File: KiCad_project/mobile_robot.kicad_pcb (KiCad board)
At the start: 2 copper layers, 90 x 62 mm, 136 parts, among them J1 IR, J10 Screw_Terminal_01x02, J11 Barrel_Jack_Switch, J12 Analog sensor, J13 Encoder A, J14 Encoder B, J15 Conn_02x05_Odd_Even, J16 Conn_02x05_Odd_Even, J17 Conn_01x03_Pin, J18 Conn_01x03_Pin, J19 Conn_02x08_Odd_Even, J2 PROGRAMING, J20 i2c, J3 Conn_01x03_Pin, J4 Conn_01x02_Pin, J5 i2c, J6 STLINK, J7 Conn_01x03_Pin, J8 UART (bluetooth), J9 Analog sensor, M1 Motor_DC, M2 Motor_DC, SW1 SW_Reset, SW2 SW_SPDT_321, U1 STM32G431RBTx, U10 TPS54202DDC, U12 TSOP321xx, U2 DRV8870DDA, U4 DRV8870DDA, U7 fuse, U8 TPS5450DDAR, U9 TPS54202DDC, Y1 Crystal_GND24

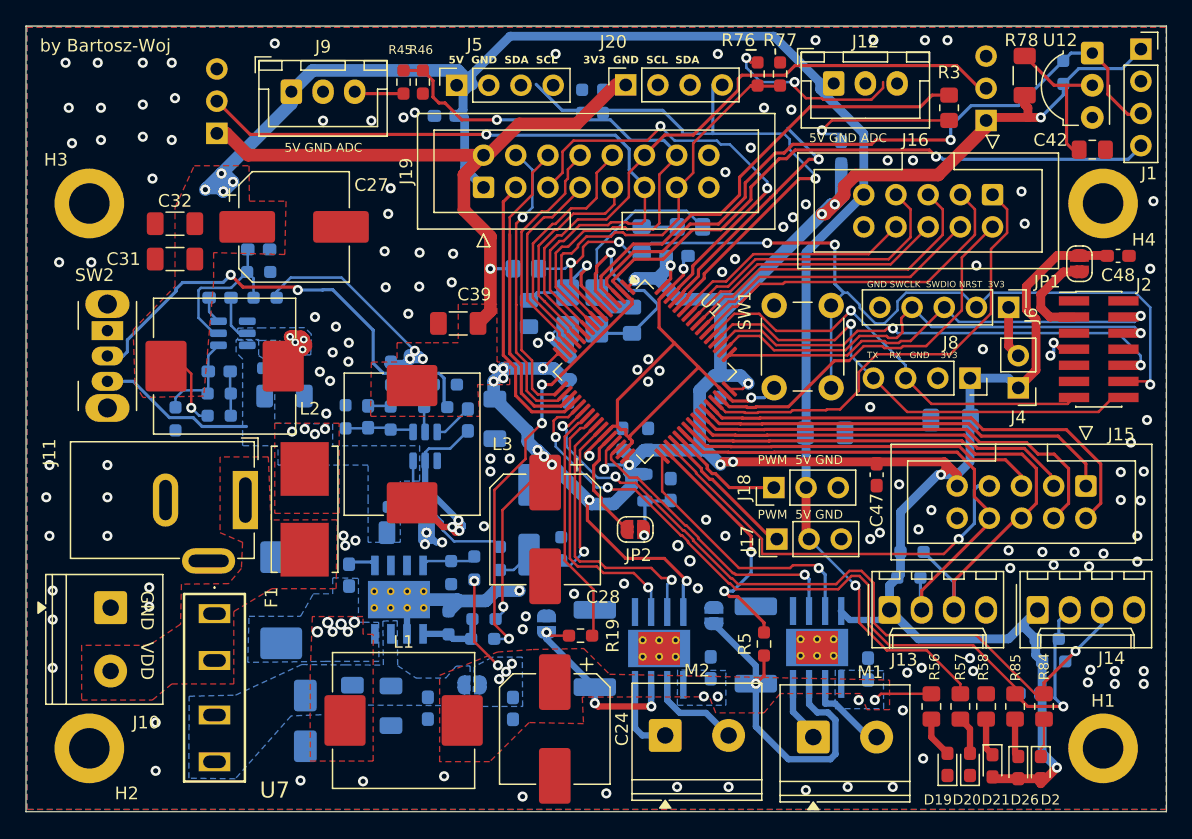
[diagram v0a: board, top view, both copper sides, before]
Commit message: bug solving
- DRC error solving related with I2C pull-up resistors
- updating readme
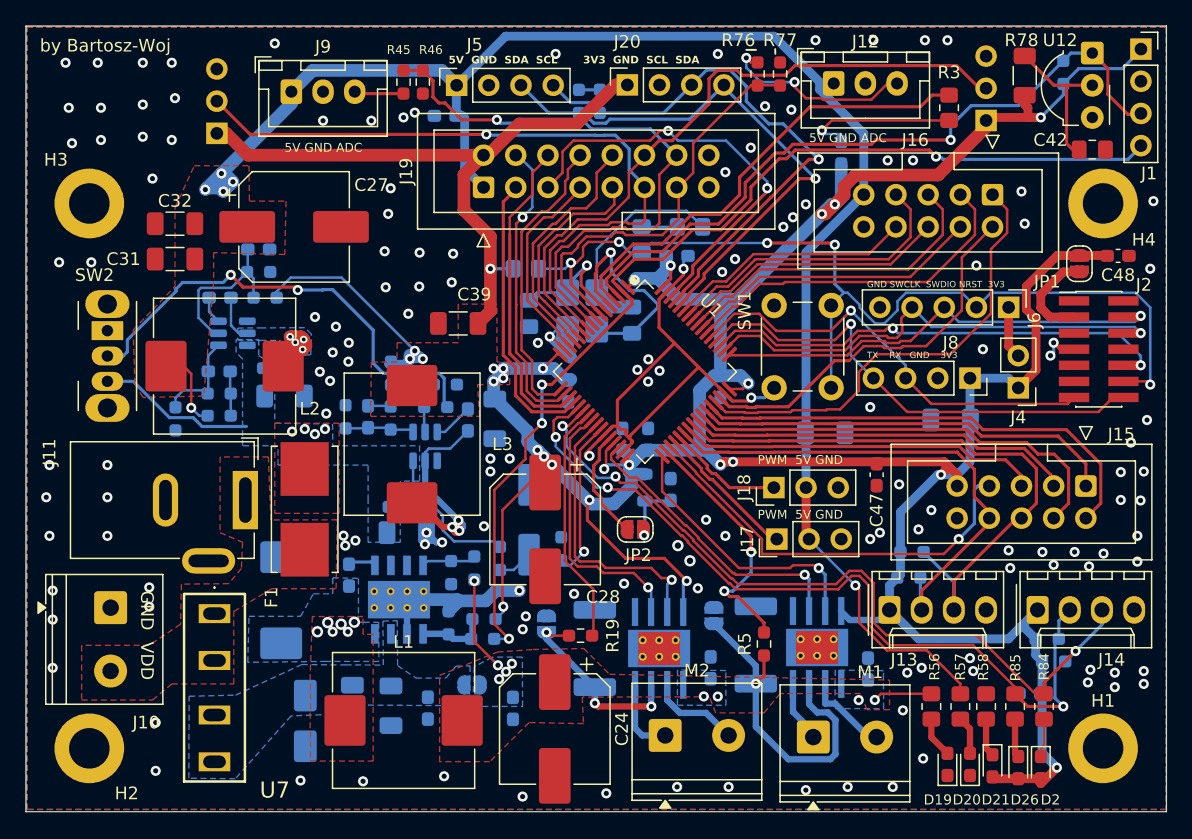
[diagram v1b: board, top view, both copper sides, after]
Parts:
- moved R10 0.25 mm to (145.3, 43.9)
- moved R9 0.25 mm to (143.6, 43.9)
- moved J20 0.13 mm to (147.5, 42.6)
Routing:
- net /i2c_SCL: track 19.8 -> 43.2 mm
- net +3.3V: track 322.2 -> 327.0 mm
- net +5V: track 136.7 -> 135.7 mm
- net /Sensor5: track 51.5 -> 52.4 mm
- net Net-(J12-Pin_3): track 14.2 -> 15.1 mm
- net /i2c_SDA: track 45.0 -> 44.0 mm

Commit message: update routing, changed IR sensor with pinout, rotate right sensor connector (bottom side)
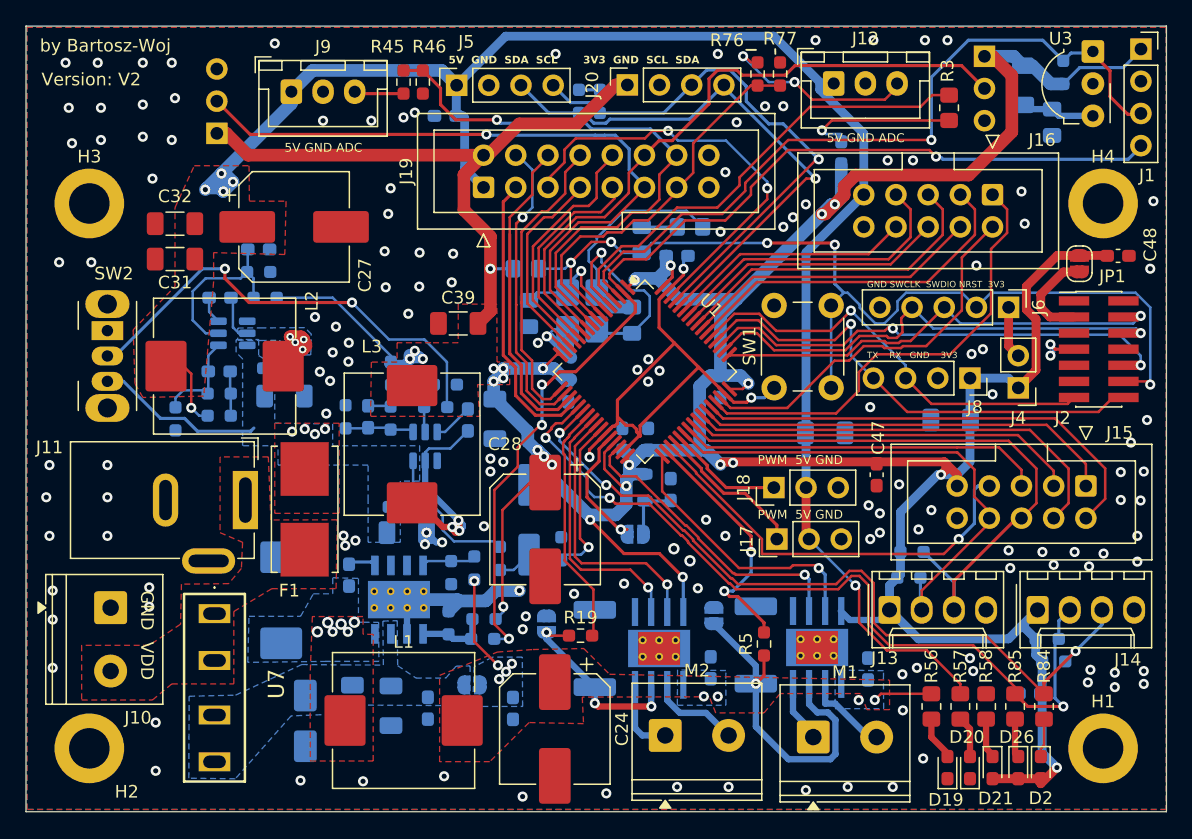
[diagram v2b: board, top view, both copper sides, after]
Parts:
- removed U12: TSOP321xx, footprint_library:Vishay_MOLD-3Pin
- added U3: VS1838B, footprint_library:Vishay_MOLD-3Pin, F.Cu at (184.2, 40.0)
- C1, C3, C4: footprint footprint_library:C_0805_2012Metric_Pad1.18x1.45mm_HandSolder -> Capacitor_SMD:C_0805_2012Metric_Pad1.18x1.45mm_HandSolder
- C11, C2, C22, C23, C25, C26, C30, C33, C34, C35, C37, C40, C44, C46, C47, C48, C9: footprint footprint_library:C_0603_1608Metric_Pad1.08x0.95mm_HandSolder -> Capacitor_SMD:C_0603_1608Metric_Pad1.08x0.95mm_HandSolder
- C20, C21, C29, C31, C32, C36, C38, C39, C41, C45: footprint footprint_library:C_1206_3216Metric_Pad1.33x1.80mm_HandSolder -> Capacitor_SMD:C_1206_3216Metric_Pad1.33x1.80mm_HandSolder
- C24, C27, C28: footprint footprint_library:CP_Elec_8x10.5 -> Capacitor_SMD:CP_Elec_8x10.5
- C42: footprint footprint_library:C_0805_2012Metric_Pad1.18x1.45mm_HandSolder -> Capacitor_SMD:C_0805_2012Metric_Pad1.18x1.45mm_HandSolder; moved to B.Cu
- C43, C5, C6, C7, C8: value C -> 0.1uF; footprint footprint_library:C_0603_1608Metric_Pad1.08x0.95mm_HandSolder -> Capacitor_SMD:C_0603_1608Metric_Pad1.08x0.95mm_HandSolder
- D1, D19, D2, D20, D21, D26: footprint footprint_library:LED_0603_1608Metric_Pad1.05x0.95mm_HandSolder -> LED_SMD:LED_0603_1608Metric_Pad1.05x0.95mm_HandSolder
- D17: footprint footprint_library:D_SMA -> Diode_SMD:D_SMA
- D18: footprint footprint_library:D_SMC -> Diode_SMD:D_SMC
- D3: footprint footprint_library:D_MiniMELF_Handsoldering -> Diode_SMD:D_MiniMELF_Handsoldering
- F1: footprint footprint_library:Fuseholder_Littelfuse_Nano2_154x -> Fuse:Fuseholder_Littelfuse_Nano2_154x
- FB1: footprint footprint_library:L_0805_2012Metric -> Inductor_SMD:L_0805_2012Metric
- H1, H2, H3, H4: footprint footprint_library:MountingHole_3.2mm_M3_ISO14580_Pad -> MountingHole:MountingHole_3.2mm_M3_ISO14580_Pad
- J1, J20, J5, J8: footprint footprint_library:PinSocket_1x04_P2.54mm_Vertical -> Connector_PinSocket_2.54mm:PinSocket_1x04_P2.54mm_Vertical
- J10, M1, M2: footprint footprint_library:TerminalBlock_Phoenix_PT-1,5-2-5.0-H_1x02_P5.00mm_Horizontal -> TerminalBlock_Phoenix:TerminalBlock_Phoenix_PT-1,5-2-5.0-H_1x02_P5.00mm_Horizontal
- J11: footprint footprint_library:BarrelJack_GCT_DCJ200-10-A_Horizontal -> Connector_BarrelJack:BarrelJack_GCT_DCJ200-10-A_Horizontal
- J12, J9: footprint footprint_library:JST_XH_B3B-XH-A_1x03_P2.50mm_Vertical -> Connector_JST:JST_XH_B3B-XH-A_1x03_P2.50mm_Vertical
- J13, J14: footprint footprint_library:Molex_KK-254_AE-6410-04A_1x04_P2.54mm_Vertical -> Connector_Molex:Molex_KK-254_AE-6410-04A_1x04_P2.54mm_Vertical
- J15, J16: footprint footprint_library:IDC-Header_2x05_P2.54mm_Vertical -> Connector_IDC:IDC-Header_2x05_P2.54mm_Vertical
- J17, J18, J3, J7: footprint footprint_library:PinHeader_1x03_P2.54mm_Vertical -> Connector_PinHeader_2.54mm:PinHeader_1x03_P2.54mm_Vertical
- J19: footprint footprint_library:IDC-Header_2x08_P2.54mm_Vertical -> Connector_IDC:IDC-Header_2x08_P2.54mm_Vertical
- J2: footprint footprint_library:PinHeader_2x07_P1.27mm_Vertical_SMD -> Connector_PinHeader_1.27mm:PinHeader_2x07_P1.27mm_Vertical_SMD
- J4: footprint footprint_library:PinHeader_1x02_P2.54mm_Vertical -> Connector_PinHeader_2.54mm:PinHeader_1x02_P2.54mm_Vertical
- J6: footprint footprint_library:PinHeader_1x05_P2.54mm_Vertical -> Connector_PinHeader_2.54mm:PinHeader_1x05_P2.54mm_Vertical
- JP1, JP3, JP4, JP5: footprint footprint_library:SolderJumper-2_P1.3mm_Open_RoundedPad1.0x1.5mm -> Jumper:SolderJumper-2_P1.3mm_Open_RoundedPad1.0x1.5mm
- JP2: footprint footprint_library:SolderJumper-2_P1.3mm_Open_RoundedPad1.0x1.5mm -> Jumper:SolderJumper-2_P1.3mm_Open_RoundedPad1.0x1.5mm; moved to B.Cu
- L1, L2, L3: footprint footprint_library:L_TechFuse_SL1040 -> Inductor_SMD:L_TechFuse_SL1040
- R1, R10, R19, R45, R46, R47, R48, R49, R5, R50, R51, R52, R53, R54, R55, R59, R60, R61, R62, R63, R7, R76, R77, R79, R8, R80, R81, R82, R83, R9: footprint footprint_library:R_0603_1608Metric_Pad0.98x0.95mm_HandSolder -> Resistor_SMD:R_0603_1608Metric_Pad0.98x0.95mm_HandSolder
- R2, R3, R4, R56, R57, R58, R84, R85: footprint footprint_library:R_0805_2012Metric_Pad1.20x1.40mm_HandSolder -> Resistor_SMD:R_0805_2012Metric_Pad1.20x1.40mm_HandSolder
- R20, R6: footprint footprint_library:R_2512_6332Metric_Pad1.40x3.35mm_HandSolder -> Resistor_SMD:R_2512_6332Metric_Pad1.40x3.35mm_HandSolder
- R78: footprint footprint_library:R_1206_3216Metric_Pad1.30x1.75mm_HandSolder -> Resistor_SMD:R_1206_3216Metric_Pad1.30x1.75mm_HandSolder; moved to B.Cu
- SW1: footprint footprint_library:SW_PUSH_6mm -> Button_Switch_THT:SW_PUSH_6mm
- SW2: footprint footprint_library:SW_Slide_SPDT_Angled_CK_OS102011MA1Q -> Button_Switch_THT:SW_Slide_SPDT_Angled_CK_OS102011MA1Q
- U1: footprint footprint_library:LQFP-64_10x10mm_P0.5mm -> Package_QFP:LQFP-64_10x10mm_P0.5mm
- U10, U9: footprint footprint_library:SOT-23-6 -> Package_TO_SOT_SMD:SOT-23-6
- U2, U4: footprint footprint_library:Texas_HTSOP-8-1EP_3.9x4.9mm_P1.27mm_EP2.95x4.9mm_Mask2.4x3.1mm_ThermalVias -> Package_SO:Texas_HTSOP-8-1EP_3.9x4.9mm_P1.27mm_EP2.95x4.9mm_Mask2.4x3.1mm_ThermalVias
- U7: footprint footprint_library:01000063Zfuse -> BW-footprints-library:01000063Zfuse
- U8: footprint footprint_library:CONV_TPS5450DDAR -> BW-footprints-library:CONV_TPS5450DDAR
- Y1: footprint footprint_library:Crystal_SMD_3225-4Pin_3.2x2.5mm_HandSoldering -> Crystal:Crystal_SMD_3225-4Pin_3.2x2.5mm_HandSoldering
- moved J7 5.07 mm to (175.6, 40.4), turned to 180 degrees
- moved C42 3.84 mm to (181.0, 45.6), turned to -90 degrees
- moved R78 0.77 mm to (178.7, 42.7), turned to 90 degrees
- moved JP2 0.38 mm to (148.1, 78.1)
- moved D19 0.25 mm to (172.7, 96.5)
- moved D20 0.25 mm to (174.5, 96.5)
- moved D21 0.14 mm to (176.3, 96.5)
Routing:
- net Net-(U3-Vs): track 12.3 -> 5.86 mm
- net +3.3V: track 327.0 -> 331.2 mm, vias 27 -> 26
- net /IR_IN: track 55.8 -> 59.8 mm
- net GND: track 85.2 -> 87.8 mm, vias 147 -> 150
- net /Sensor8: track 32.0 -> 30.4 mm
- net /Sensor6: track 56.0 -> 54.5 mm
- net Net-(JP2-B): track 8.81 -> 10.3 mm, vias 0 -> 1
- net Net-(U1-PF1): track 10.6 -> 9.29 mm
- net /Sensor7: track 47.1 -> 45.8 mm
- net /KILL_PIN: track 82.8 -> 84.0 mm
- net /STATUS LED3: track 64.5 -> 65.5 mm
- net Net-(U9-EN): track 12.7 -> 13.7 mm
- net /Power section/V_IN_CHK: track 24.0 -> 24.8 mm
- net Net-(SW2-B): track 37.4 -> 36.7 mm
- net /PWM_M1_A: track 22.2 -> 21.5 mm
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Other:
- board text added: "Version: V2"

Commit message: update GND routing
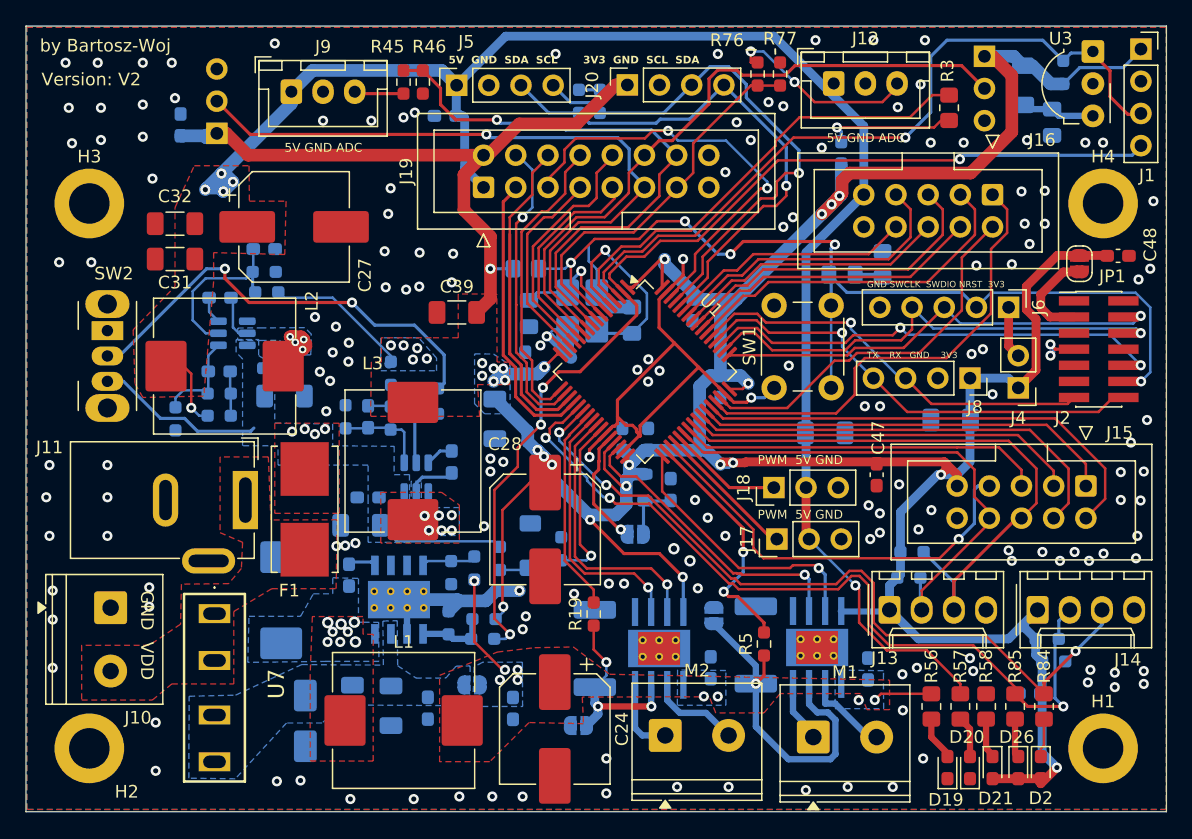
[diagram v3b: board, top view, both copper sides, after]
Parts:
- added C10: 0.1uF, Capacitor_SMD:C_0603_1608Metric_Pad1.08x0.95mm_HandSolder, B.Cu at (112.2, 45.8)
- D3: footprint Diode_SMD:D_MiniMELF_Handsoldering -> Diode_SMD:D_MiniMELF
- moved C1 16.0 mm to (164.4, 57.6), turned to 0 degrees
- moved R4 15.5 mm to (167.6, 56.8), turned to 90 degrees
- moved JP4 8.39 mm to (143.6, 93.2), turned to 0 degrees
- moved C8 4.44 mm to (152.6, 60.4), turned to -90 degrees
- moved C6 4.05 mm to (139.4, 64.6), turned to 90 degrees
- moved C36 3.69 mm to (126.4, 77.4), turned to 180 degrees
- moved C35 3.55 mm to (133.6, 72.4)
- moved R61 2.75 mm to (131.6, 68.6)
- moved C37 2.65 mm to (127.0, 75.2), turned to 180 degrees
- moved U10 2.53 mm to (130.8, 73.6)
- moved D3 2.04 mm to (139.8, 79.0)
- moved R19 2.00 mm to (144.8, 84.4), turned to 90 degrees
- moved R59 1.64 mm to (131.6, 66.6)
- moved L3 1.33 mm to (130.5, 72.3)
- moved C39 0.88 mm to (134.0, 60.6)
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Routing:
- net Net-(U10-SW): track 19.1 -> 3.80 mm, vias 3 -> 6
- net GND: track 87.8 -> 75.1 mm, vias 150 -> 163
- net +3.3V: track 331.2 -> 324.2 mm, vias 26 -> 30
- net /M_1_SENSE: track 19.3 -> 16.5 mm
- net /UART_TX: track 38.8 -> 37.0 mm
- net Net-(U10-EN): track 4.09 -> 5.91 mm
- net /i2c_SDA: track 43.7 -> 42.0 mm
- net Net-(U10-FB): track 5.49 -> 7.21 mm
- net Net-(D1-K): track 11.4 -> 9.71 mm
- net /UART_RX: track 34.4 -> 32.8 mm
- net /Power section/V_IN_CHK: track 24.8 -> 23.4 mm
- net Net-(SW2-B): track 36.7 -> 35.6 mm
- net /KILL_PIN: track 84.0 -> 83.0 mm
- net Net-(U10-BOOT): track 3.17 -> 2.23 mm
- net Net-(JP2-B): track 10.3 -> 9.33 mm
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- added copper zone on B.Cu, net +3.3V
- added copper zone on B.Cu, net Net-(U10-SW)
- added copper zone on F.Cu, net Net-(U10-SW)
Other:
- board text added: "GND ADC 3V3"
